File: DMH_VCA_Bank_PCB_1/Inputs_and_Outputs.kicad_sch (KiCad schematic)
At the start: 36 parts, among them J0 Conn_01x01, J1 TS_Jack_6.35mm_Sw, J10 TS_Jack_6.35mm_Sw, J2 TS_Jack_6.35mm_Sw, J200 IDC_02x05, J3 TS_Jack_6.35mm_Sw, J4 TS_Jack_6.35mm_Sw, J5 TS_Jack_6.35mm_Sw, J50 Conn_01x08, J6 TS_Jack_6.35mm_Sw, J60 Conn_01x08, J7 TS_Jack_6.35mm_Sw, J70 Conn_01x08, J8 TS_Jack_6.35mm_Sw, J9 TS_Jack_6.35mm_Sw, SW1 SW_DPDT, SW2 SW_DPDT, SW3 SW_DPDT

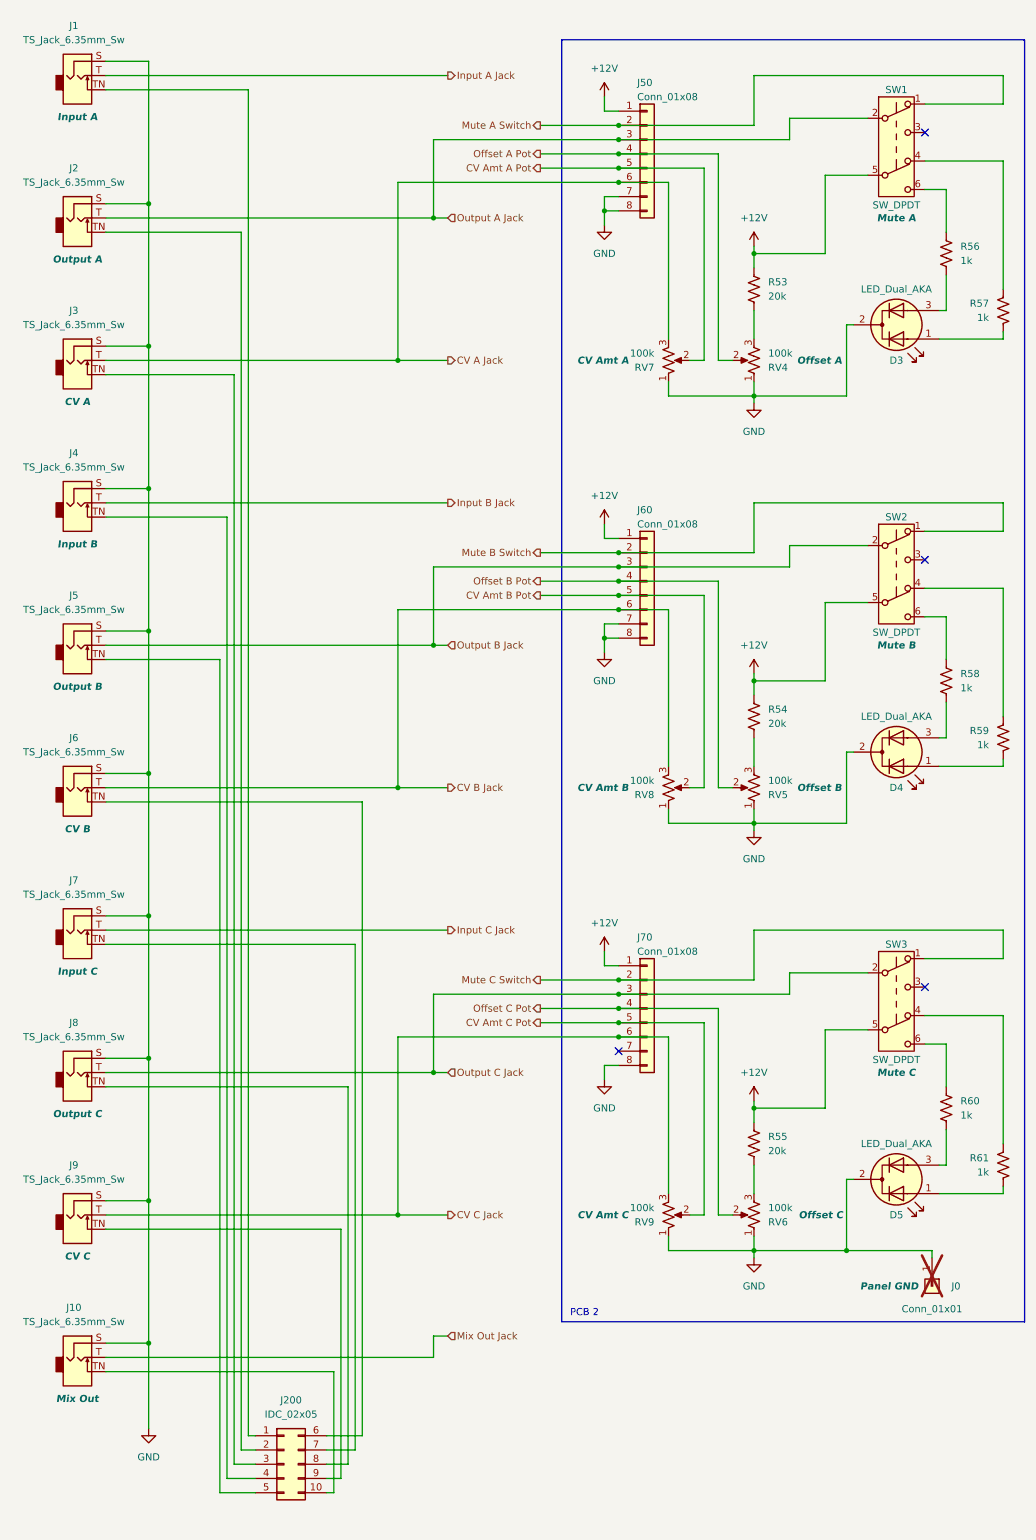
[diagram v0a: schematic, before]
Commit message: Finished schematic of PCB 1
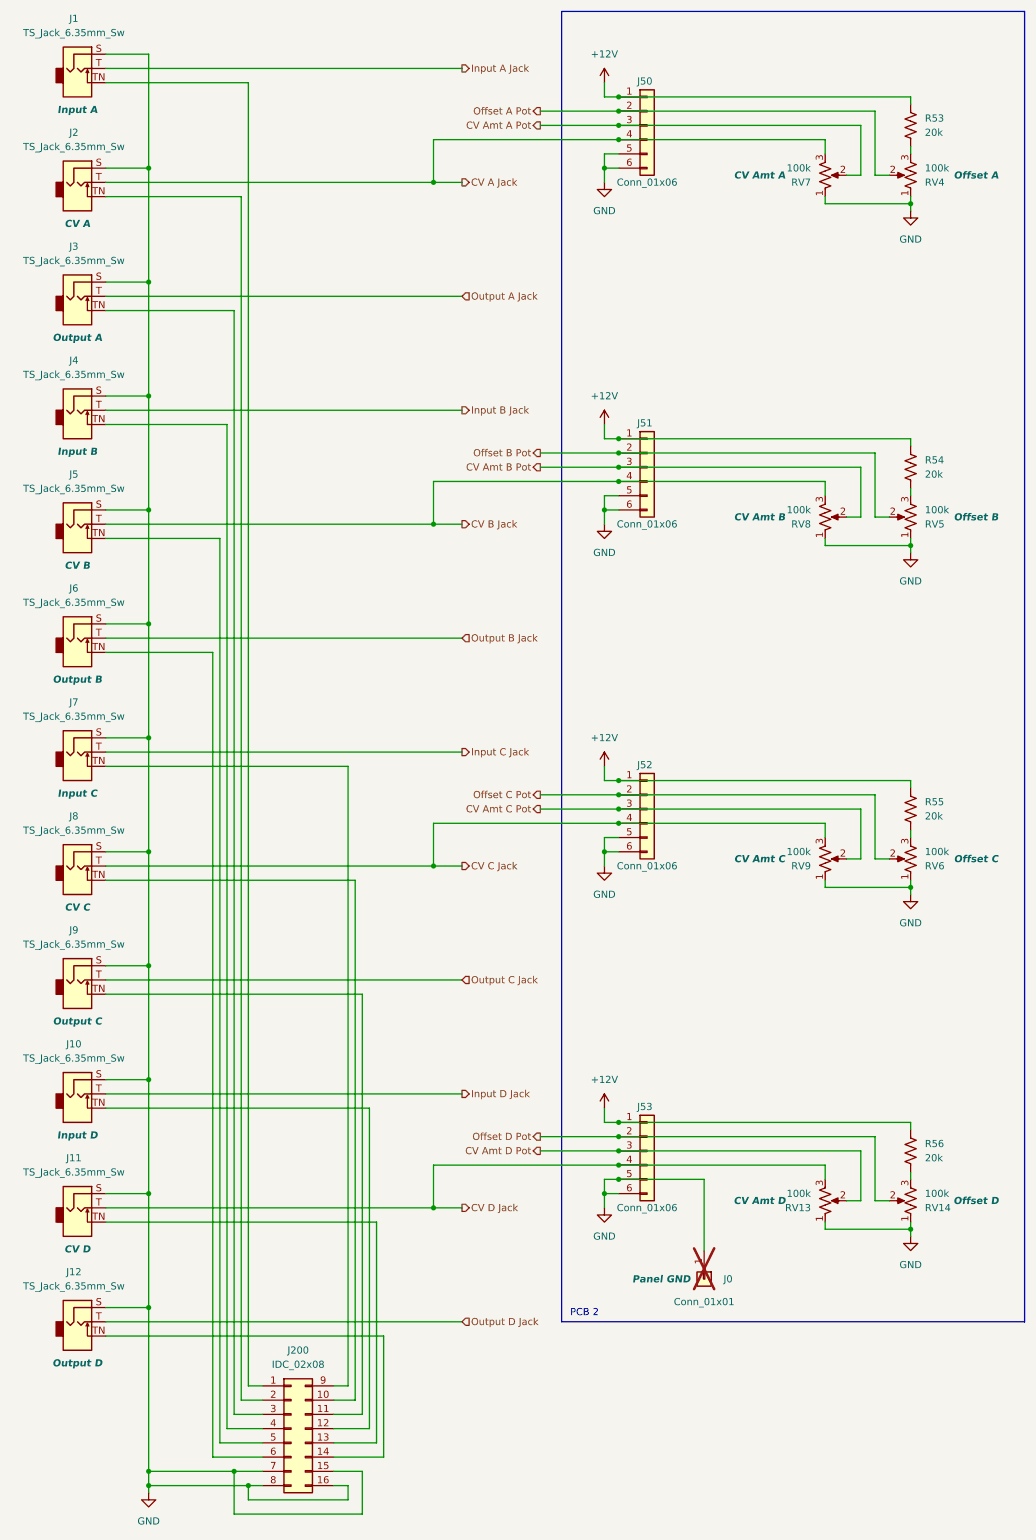
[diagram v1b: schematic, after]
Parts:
- removed D3, D4, D5: LED_Dual_AKA, SynthStuff:LED_D3.0mm-2color, symbol Device:LED_Dual_AKA
- removed J60, J70: Conn_01x08, Connector_PinSocket_2.54mm:PinSocket_1x08_P2.54mm_Vertical, symbol Connector_Generic:Conn_01x08
- removed R57, R58, R59, R60, R61: 1k, Resistor_THT:R_Axial_DIN0207_L6.3mm_D2.5mm_P7.62mm_Horizontal, symbol Device:R_US
- removed SW1, SW2, SW3: SW_DPDT, SynthStuff:Toggle_Switch_2_Poles_TE, symbol SynthStuff:Switch_DPDT
- added J11, J12: TS_Jack_6.35mm_Sw, SynthStuff:CUI_MJ-63052A, symbol SynthStuff:TS_Jack_6.35mm_Sw
- added J51, J52, J53: Conn_01x06, Connector_PinSocket_2.54mm:PinSocket_1x08_P2.54mm_Vertical, symbol Connector_Generic:Conn_01x06
- added RV13: 100k, SynthStuff:Potentiometer_TT_P110KH1, symbol Device:R_Potentiometer_US
- added RV14: 100k, SynthStuff:Potentiometer_Alpha_RD901F-40-00D_Single_Vertical, symbol Device:R_Potentiometer_US
- J10: Function Mix Out -> Input D
- J2: Function Output A -> CV A
- J200: value IDC_02x05 -> IDC_02x08; footprint SynthStuff:IDC-Header_2x05_P2.54mm_Vertical_BackBone -> SynthStuff:IDC-Header_2x08_P2.54mm_Vertical_BackBone; symbol SynthStuff:BackBone_Connector_10Pin -> SynthStuff:BackBone_Connector_16Pin
- J3: Function CV A -> Output A
- J5: Function Output B -> CV B
- J50: value Conn_01x08 -> Conn_01x06; symbol Connector_Generic:Conn_01x08 -> Connector_Generic:Conn_01x06
- J6: Function CV B -> Output B
- J8: Function Output C -> CV C
- J9: Function CV C -> Output C
- R56: value 1k -> 20k
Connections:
- net Mute A Switch is gone; now on net Offset A Pot: J50.2 (Pin_2)
- net +12V: now also R56.2, J51.1 (Pin_1), J52.1 (Pin_1), J53.1 (Pin_1)
- net CV A Jack: now also J2.T, J50.4 (Pin_4); no longer J3.T, J50.6 (Pin_6)
- net CV Amt A Pot: now also J50.3 (Pin_3); no longer J50.5 (Pin_5)
- net CV Amt B Pot: now also J51.3 (Pin_3)
- net CV Amt C Pot: now also J52.3 (Pin_3)
- net CV B Jack: now also J5.T, J51.4 (Pin_4); no longer J6.T
- net CV C Jack: now also J8.T, J52.4 (Pin_4); no longer J9.T
- net GND: now also J200.15 (Pin_15), J200.16 (Pin_16), J200.7 (Pin_7), J200.8 (Pin_8), J50.5 (Pin_5), J50.6 (Pin_6), J11.S, J12.S, J51.5 (Pin_5), J51.6 (Pin_6), J52.5 (Pin_5), J52.6 (Pin_6), J53.5 (Pin_5), J53.6 (Pin_6), RV13.1, RV14.1; no longer J50.7 (Pin_7), J50.8 (Pin_8)
- net Offset A Pot: no longer J50.4 (Pin_4)
- net Offset B Pot: now also J51.2 (Pin_2)
- net Offset C Pot: now also J52.2 (Pin_2)
- net Output A Jack: now also J3.T; no longer J2.T, J50.3 (Pin_3)
- net Output B Jack: now also J6.T; no longer J5.T
- net Output C Jack: now also J9.T; no longer J8.T
- net at J9.TN: now also J200.11 (Pin_11); no longer J200.9 (Pin_9)
- net at J200.10 (Pin_10): now also J8.TN; no longer J10.TN
- net at J7.TN: now also J200.9 (Pin_9); no longer J200.7 (Pin_7)
- net at R56.1: now also RV14.3
- net Mix Out Jack renamed Input D Jack
- new net: J10.TN, J200.12 (Pin_12)
- new net: J11.TN, J200.13 (Pin_13)
- new net: J12.TN, J200.14 (Pin_14)
- new net CV Amt D Pot: J53.3 (Pin_3), RV13.2
- new net CV D Jack: J11.T, J53.4 (Pin_4), RV13.3
- new net Offset D Pot: J53.2 (Pin_2), RV14.2
- new net Output D Jack: J12.T
- no-connect marks 4 -> 0
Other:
- moved on the sheet: J0, J1, J10, J2, J3, J4, J5, J6, J7, J8, J9, R53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
